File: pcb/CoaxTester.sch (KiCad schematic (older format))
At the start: 34 parts

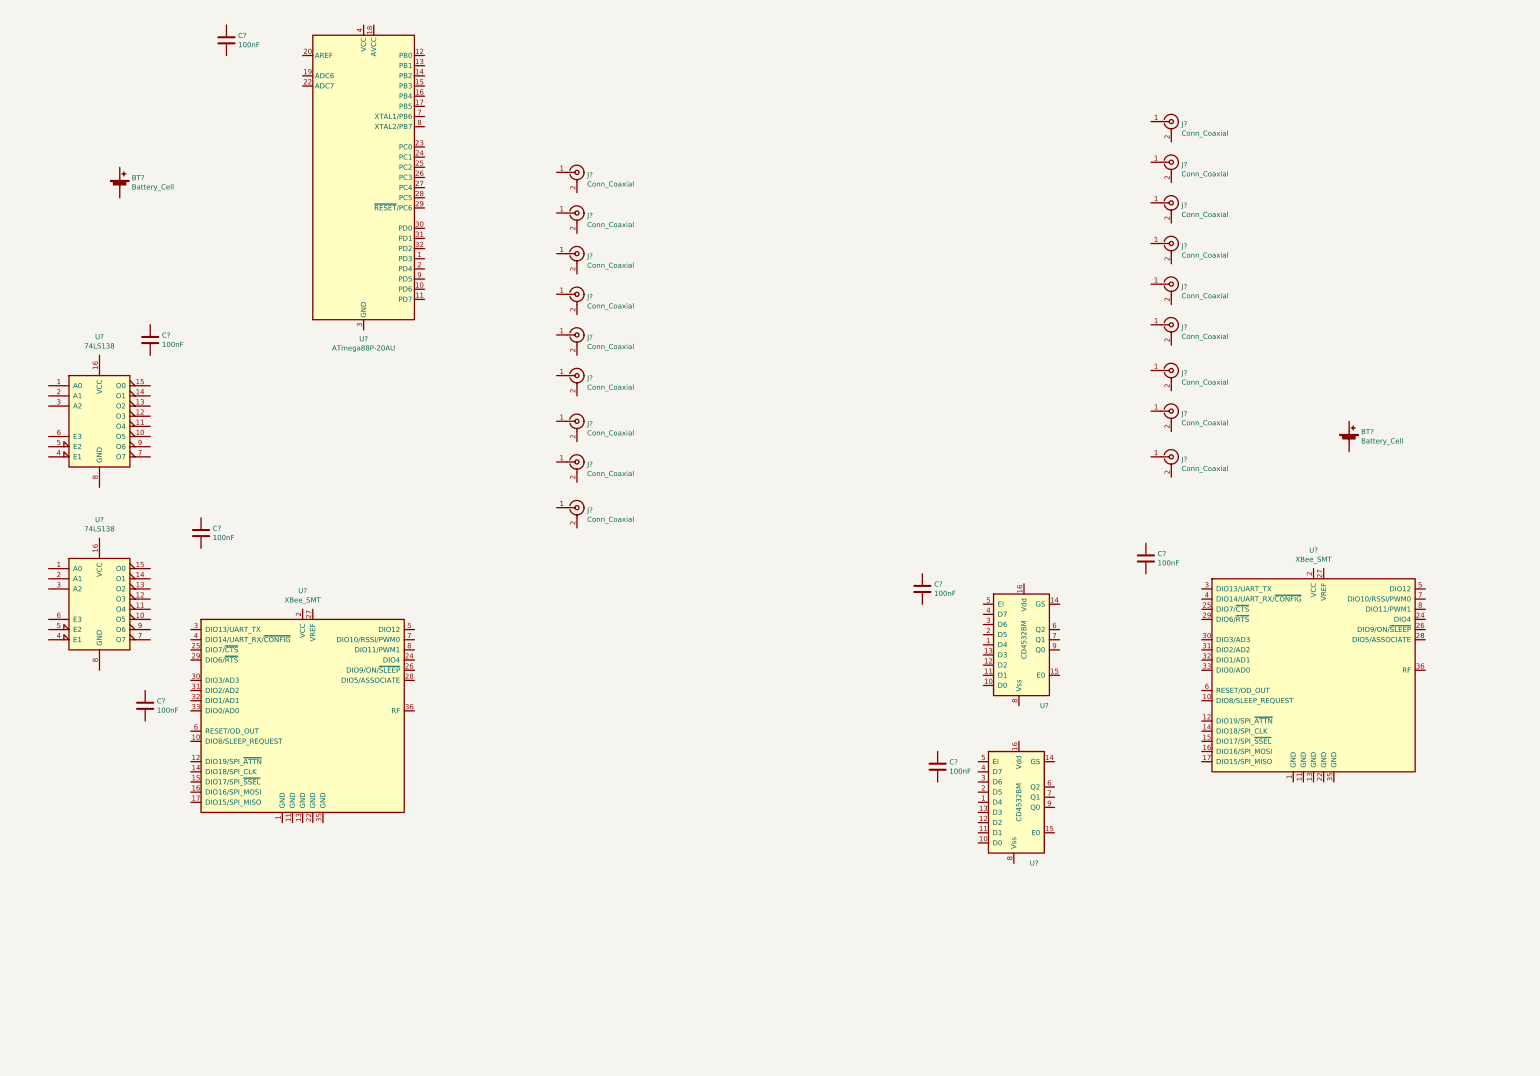
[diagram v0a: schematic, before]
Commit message: Adds a bit more to the schematic - power module is done
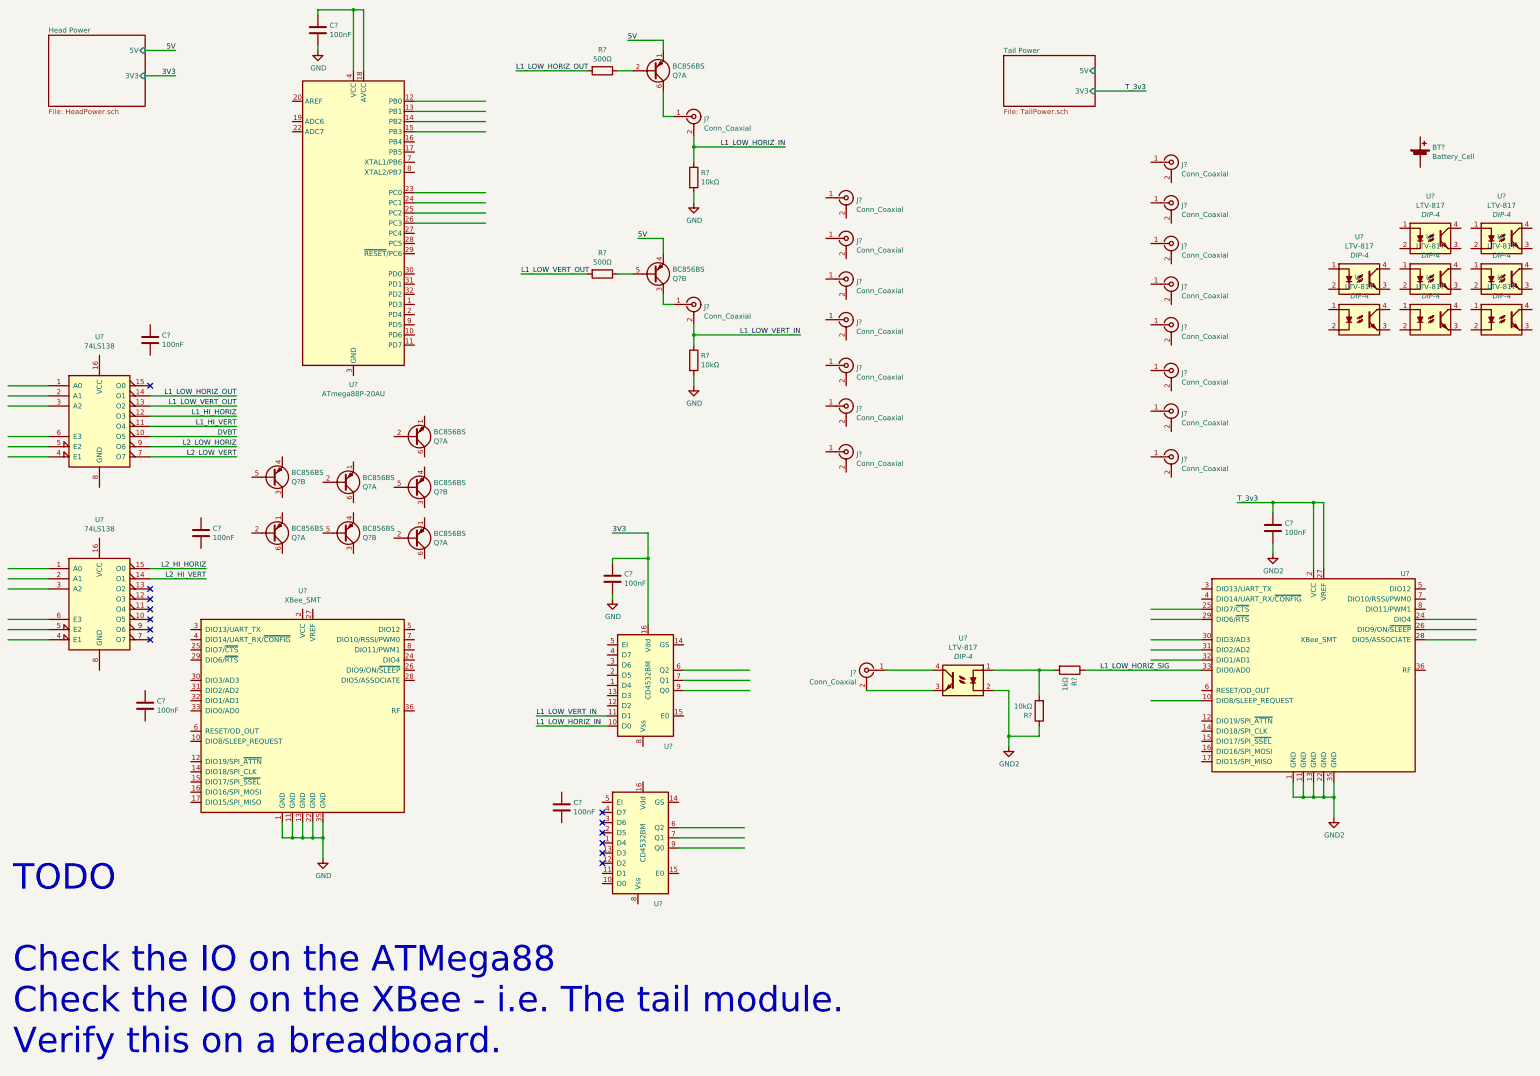
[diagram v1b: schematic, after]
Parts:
- removed BT?: Battery_Cell, Connector_PinHeader_2.54mm:PinHeader_1x02_P2.54mm_Vertical, symbol Device:Battery_Cell
- removed C? (x2): 100nF, symbol Device:C
- removed U? (x2): CD4532BM, Package_SO:SO-16_3.9x9.9mm_P1.27mm, symbol CoaxTester:CD4532BM
- added C? (x2): 100nF, symbol Device:C
- added Q? (x9): BC856BS, Package_TO_SOT_SMD:SOT-363_SC-70-6, symbol Transistor_BJT:BC856BS
- added R? (x2): 500Ω, symbol Device:R
- added R? (x3): 10kΩ, symbol Device:R
- added R?: 1kΩ, symbol Device:R
- added U? (x9): LTV-817, DIP-4, symbol CoaxTester:LTV-817
- added U? (x2): CD4532BM, Package_SO:SO-16_3.9x9.9mm_P1.27mm, symbol CoaxTester:CD4532BM
- BT?: footprint Connector_PinHeader_2.54mm:PinHeader_1x02_P2.54mm_Vertical -> CoaxTester:BATT_CONN
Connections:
- net labels added: 3V3, 5V, DVBT, GND, GND2, L1_HI_HORIZ, L1_HI_VERT, L1_LOW_HORIZ_IN, L1_LOW_HORIZ_OUT, L1_LOW_HORIZ_SIG, L1_LOW_VERT_IN, L1_LOW_VERT_OUT, L2_HI_HORIZ, L2_HI_VERT, L2_LOW_HORIZ, L2_LOW_VERT, T_3v3
- wire segments 0 -> 119
- no-connect marks 0 -> 13
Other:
- note added: "TODO\n\nCheck the IO on the ATMega88\nCheck the IO on the XBee - i.e. The tail module.\nVerify this on a breadboard."
- moved on the sheet: BT?, C?, J?, U?

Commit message: Adds more to the schematic
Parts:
- removed BT?: Battery_Cell, CoaxTester:BATT_CONN, symbol Device:Battery_Cell
- removed C? (x4): 100nF, symbol Device:C
- removed J? (x18): Conn_Coaxial, CoaxTester:FB_EPG, symbol Connector:Conn_Coaxial
- removed Q? (x9): BC856BS, Package_TO_SOT_SMD:SOT-363_SC-70-6, symbol Transistor_BJT:BC856BS
- removed R? (x2): 500Ω, symbol Device:R
- removed R? (x3): 10kΩ, symbol Device:R
- removed R?: 1kΩ, symbol Device:R
- removed U? (x2): 74LS138, Package_SO:SO-16_3.9x9.9mm_P1.27mm, symbol 74xx:74LS138
- removed U?: ATmega88P-20AU, Package_QFP:TQFP-32_7x7mm_P0.8mm, symbol MCU_Microchip_ATmega:ATmega88P-20AU
- removed U? (x9): LTV-817, DIP-4, symbol CoaxTester:LTV-817
- removed U? (x2): CD4532BM, Package_SO:SO-16_3.9x9.9mm_P1.27mm, symbol CoaxTester:CD4532BM
- added J?: PRG_HEADER, symbol Connector_Generic:Conn_02x03_Odd_Even
- added Q? (x2): IRLML2502, Micro3, symbol Tfac-Symbols:IRLML2502
- added R? (x2): 0Ω, symbol Device:R
- added R? (x3): 10kΩ, symbol Device:R
- added U?: ATmega88-20AU, Package_QFP:TQFP-32_7x7mm_P0.8mm, symbol MCU_Microchip_ATmega:ATmega88-20AU
- C? (x3): footprint (none) -> Capacitor_SMD:C_0805_2012Metric
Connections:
- net labels added: DIN0, DIN1, DIN2, DIN3, DOUT0, DOUT1, DOUT2, DOUT3, MISO, MOSI, Rx_H, Rx_L, SCK, TA_HORIZ, TA_VERT, TB_HORIZ, TB_VERT, TC_HORIZ, TC_VERT, T_SIG, Tx_H, Tx_L, ~RESET
- net labels removed: DVBT, L1_HI_HORIZ, L1_HI_VERT, L1_LOW_HORIZ_IN, L1_LOW_HORIZ_OUT, L1_LOW_HORIZ_SIG, L1_LOW_VERT_IN, L1_LOW_VERT_OUT, L2_HI_HORIZ, L2_HI_VERT, L2_LOW_HORIZ, L2_LOW_VERT
- wire segments 119 -> 138
- no-connect marks 13 -> 33
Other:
- note added: "Coax Driver"
- note added: "Level Shifter"
- moved on the sheet: C?, U?

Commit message: Fixed up library reference to a local submodule
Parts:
- J?: footprint (none) -> TagConnect:PRG_TC2030-IDC-FP_TH
- R? (x5): footprint (none) -> Resistor_SMD:R_0805_2012Metric
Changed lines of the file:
@@
 F 0 "J?" H 4850 5417 50  0000 C CNN
 F 1 "PRG_HEADER" H 4850 5326 50  0000 C CNN
-F 2 "" H 4800 5100 50  0001 C CNN
+F 2 "TagConnect:PRG_TC2030-IDC-FP_TH" H 4800 5100 50  0001 C CNN
 F 3 "~" H 4800 5100 50  0001 C CNN
 	1    4800 5100
@@
 F 0 "R?" V 4550 3050 50  0000 C CNN
 F 1 "10kΩ" V 4750 3050 50  0000 C CNN
-F 2 "" V 4580 3050 50  0001 C CNN
+F 2 "Resistor_SMD:R_0805_2012Metric" V 4580 3050 50  0001 C CNN
 F 3 "~" H 4650 3050 50  0001 C CNN
 	1    4650 3050
@@
 F 0 "R?" H 2820 9196 50  0000 L CNN
 F 1 "0Ω" H 2820 9105 50  0000 L CNN
-F 2 "" V 2680 9150 50  0001 C CNN
+F 2 "Resistor_SMD:R_0805_2012Metric" V 2680 9150 50  0001 C CNN
 F 3 "~" H 2750 9150 50  0001 C CNN
 	1    2750 9150
@@
 F 0 "R?" H 3470 9196 50  0000 L CNN
 F 1 "10kΩ" H 3470 9105 50  0000 L CNN
-F 2 "" V 3330 9150 50  0001 C CNN
+F 2 "Resistor_SMD:R_0805_2012Metric" V 3330 9150 50  0001 C CNN
 F 3 "~" H 3400 9150 50  0001 C CNN
 	1    3400 9150
@@
 F 0 "R?" H 2820 7796 50  0000 L CNN
 F 1 "0Ω" H 2820 7705 50  0000 L CNN
-F 2 "" V 2680 7750 50  0001 C CNN
+F 2 "Resistor_SMD:R_0805_2012Metric" V 2680 7750 50  0001 C CNN
 F 3 "~" H 2750 7750 50  0001 C CNN
 	1    2750 7750
@@
 F 0 "R?" H 3470 7796 50  0000 L CNN
 F 1 "10kΩ" H 3470 7705 50  0000 L CNN
-F 2 "" V 3330 7750 50  0001 C CNN
+F 2 "Resistor_SMD:R_0805_2012Metric" V 3330 7750 50  0001 C CNN
 F 3 "~" H 3400 7750 50  0001 C CNN
 	1    3400 7750
